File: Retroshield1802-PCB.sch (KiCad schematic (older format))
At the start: 27 parts, among them J1 Conn_01x17, J10 Conn_01x17, J11 Conn_01x17, J12 Conn_01x17, J2 Conn_01x17, J3 Conn_01x17, J4 Conn_01x17, J5 Conn_01x17, J6 Conn_01x17, J7 Conn_01x17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

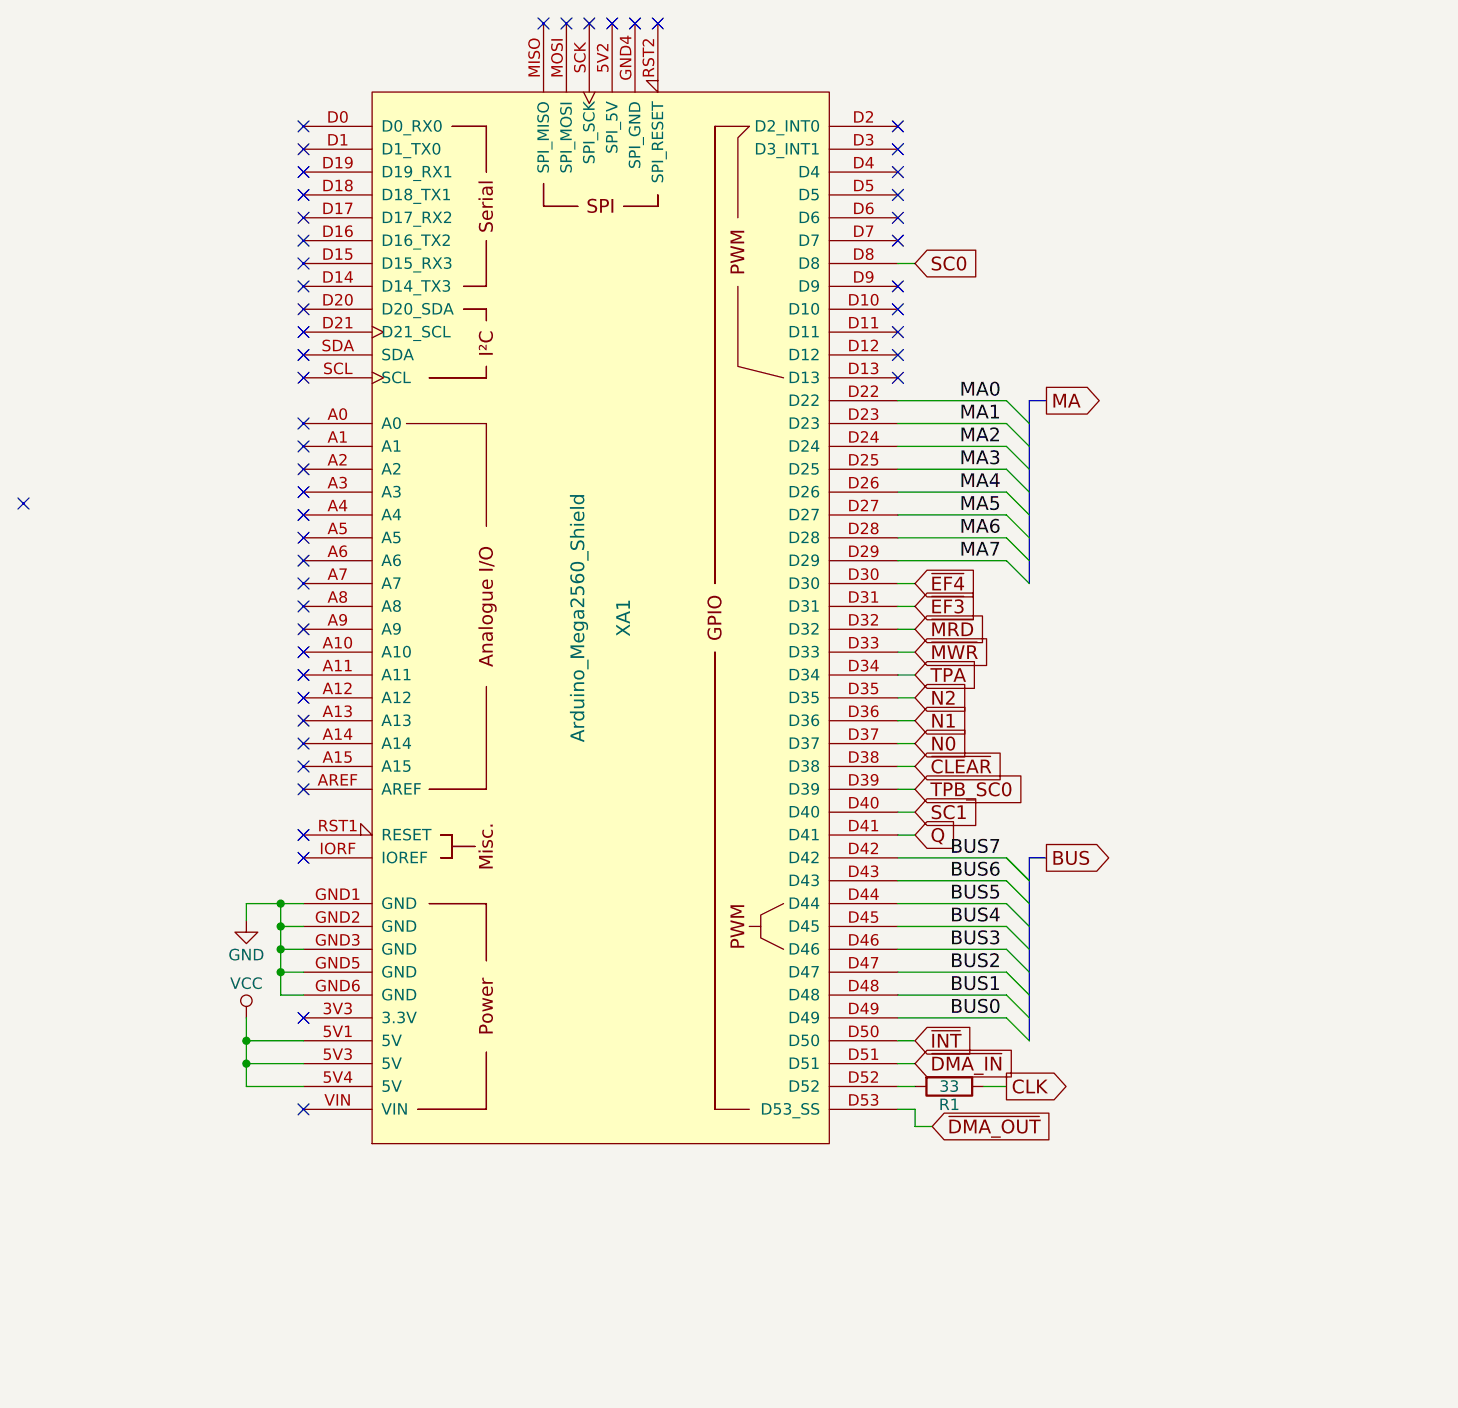
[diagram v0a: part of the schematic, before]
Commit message: Added header for 0.96" I2C displau
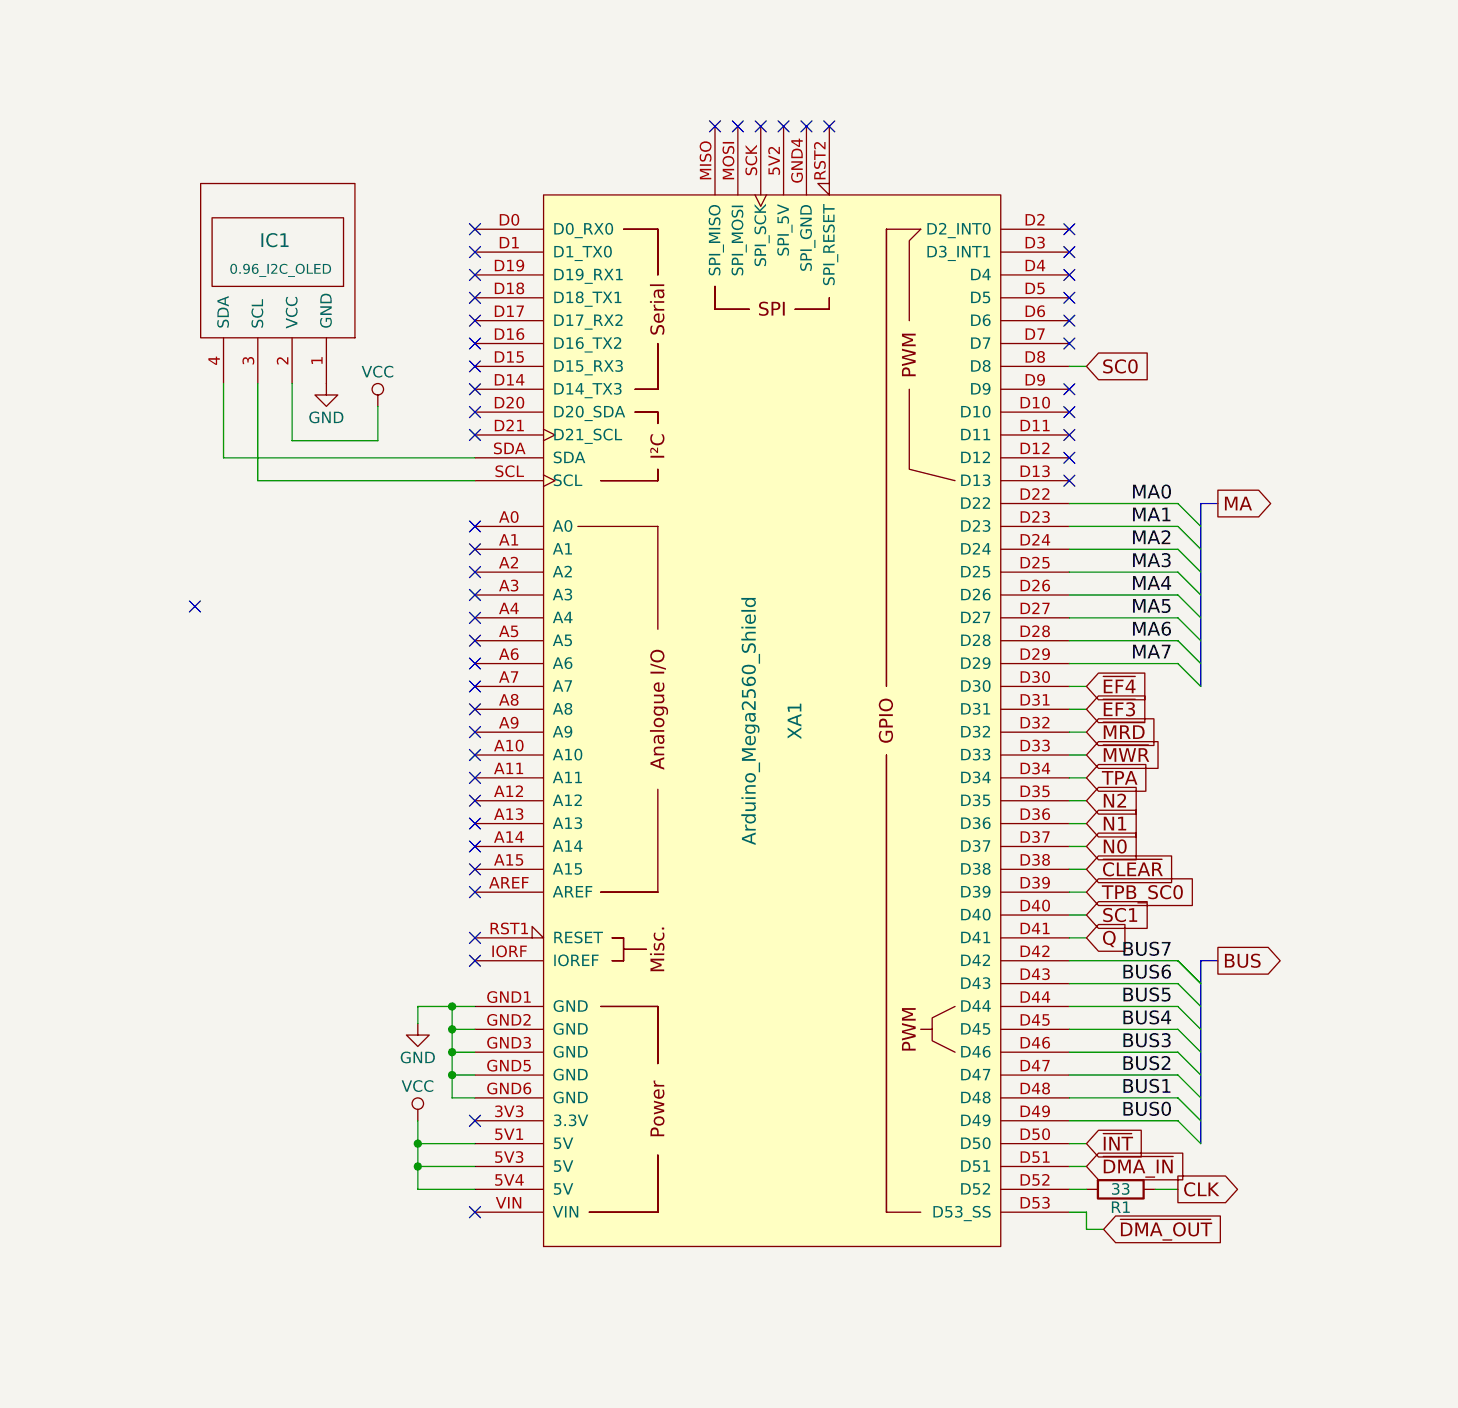
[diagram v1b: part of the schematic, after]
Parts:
- added IC1: 0.96_I2C_OLED, OLED:0.96_I2C_OLED, symbol 0.96_I2C_OLED
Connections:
- net GND: now also IC1.1 (GND)
- net VCC: now also IC1.2 (VCC)
- net at XA1.SCL: now also IC1.3 (SCL)
- net at XA1.SDA: now also IC1.4 (SDA)
- no-connect marks 256 -> 254
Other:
- moved on the sheet: R1, XA1

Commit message: Gerber export
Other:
- note added: "PCB made from the schematics provided by Erturk Kocalar, adds an 1802 processor to\nthe Arduino Mega 2560 allowing the user to run 1802-based software.\n\nFirmware and original source:\nhttps://gitlab.com/8bitforce/retroshield1802"
- note added: "RetroShield 1802 PCB"
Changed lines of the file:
@@
 Wire Wire Line
 	1375 3150 1375 2725
+Text Notes 12200 10925 0    60   ~ 0
+RetroShield 1802 PCB
+Text Notes 11850 10475 0    60   ~ 0
+PCB made from the schematics provided by Erturk Kocalar, adds an 1802 processor to\nthe Arduino Mega 2560 allowing the user to run 1802-based software.\n\nFirmware and original source:\nhttps://gitlab.com/8bitforce/retroshield1802
 $EndSCHEMATC
